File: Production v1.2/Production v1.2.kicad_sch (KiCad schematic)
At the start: 26 parts, among them IC1 MAX3323EEUE+T, J1 530480510, J2 530480410, J3 USB4085-GF-A_REVB, U1 ATSAMD21G18A-AUT, Y1 ECS-.327-12.5-1210-TR

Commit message: 1.2 routed
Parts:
- R4: value 4K7 -> 5K6
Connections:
- net AREFB is gone; now on net AREFA: U1.9 (PA04)
- net +3V3: now also C7.1, U1.17 (VDD/IO), U1.36 (VDD/IO); no longer C7.2
- net GND: now also C7.2; no longer R5.2
- net GNDANA: now also R5.2
- net OLED_CS: now also U1.19 (PB10)
- net OLED_DC: now also U1.15 (PA10); no longer U1.7 (PB08)
- net OLED_RST: now also U1.16 (PA11); no longer U1.8 (PB09)
- net RUN: now also U1.48 (PB03); no longer U1.39 (PA27)
- net SETBTN: now also U1.13 (PA08); no longer U1.3 (PA02)
- net SETLED: now also U1.10 (PA05); no longer U1.48 (PB03)
- net SOFTBTN: now also U1.24 (PA15); no longer U1.14 (PA09)
- net VDDCORE: now reaches C8.1, U1.43 (VDDCORE)

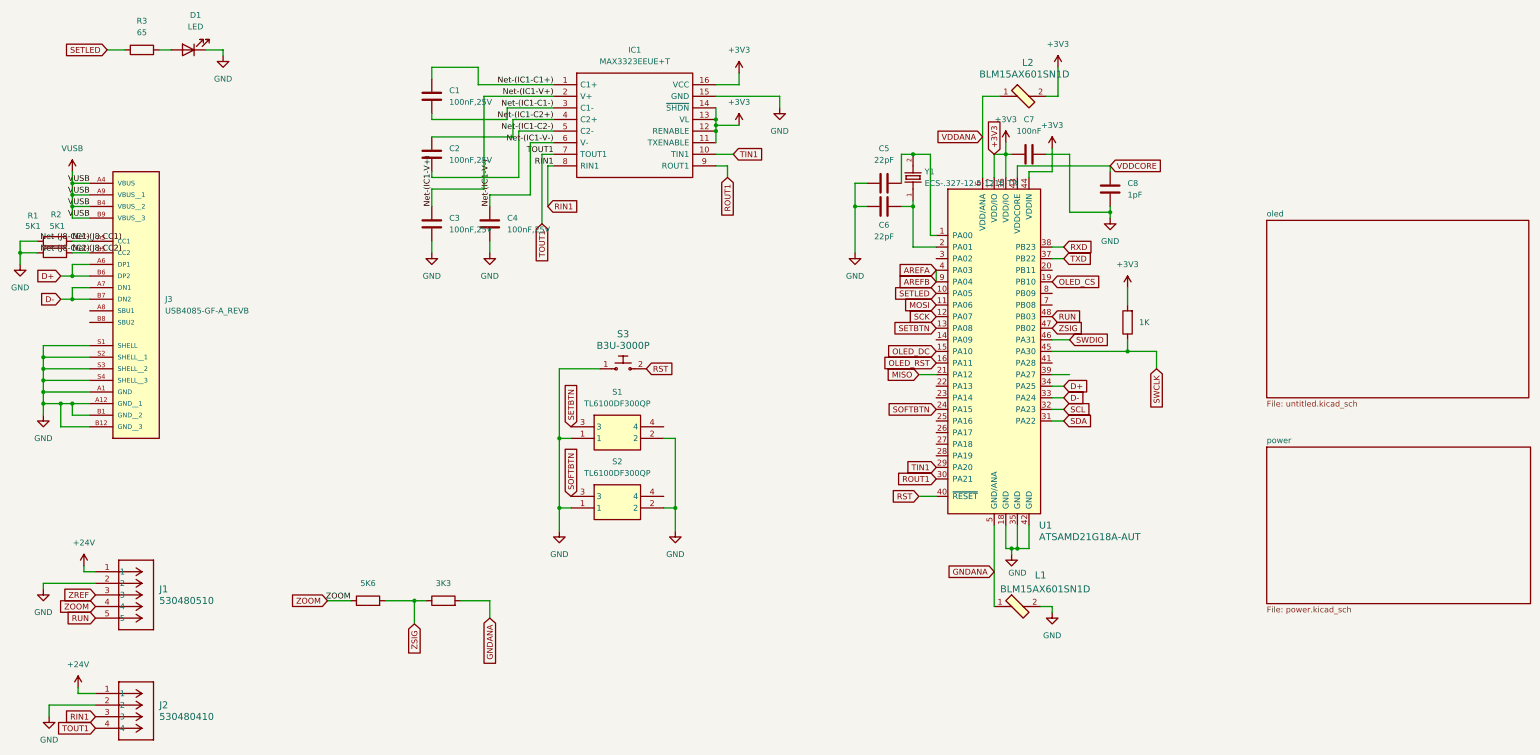
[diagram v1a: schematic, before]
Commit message: v1.2 checked & labeled
flipped fpc connector to underside, for better ribbon routing.
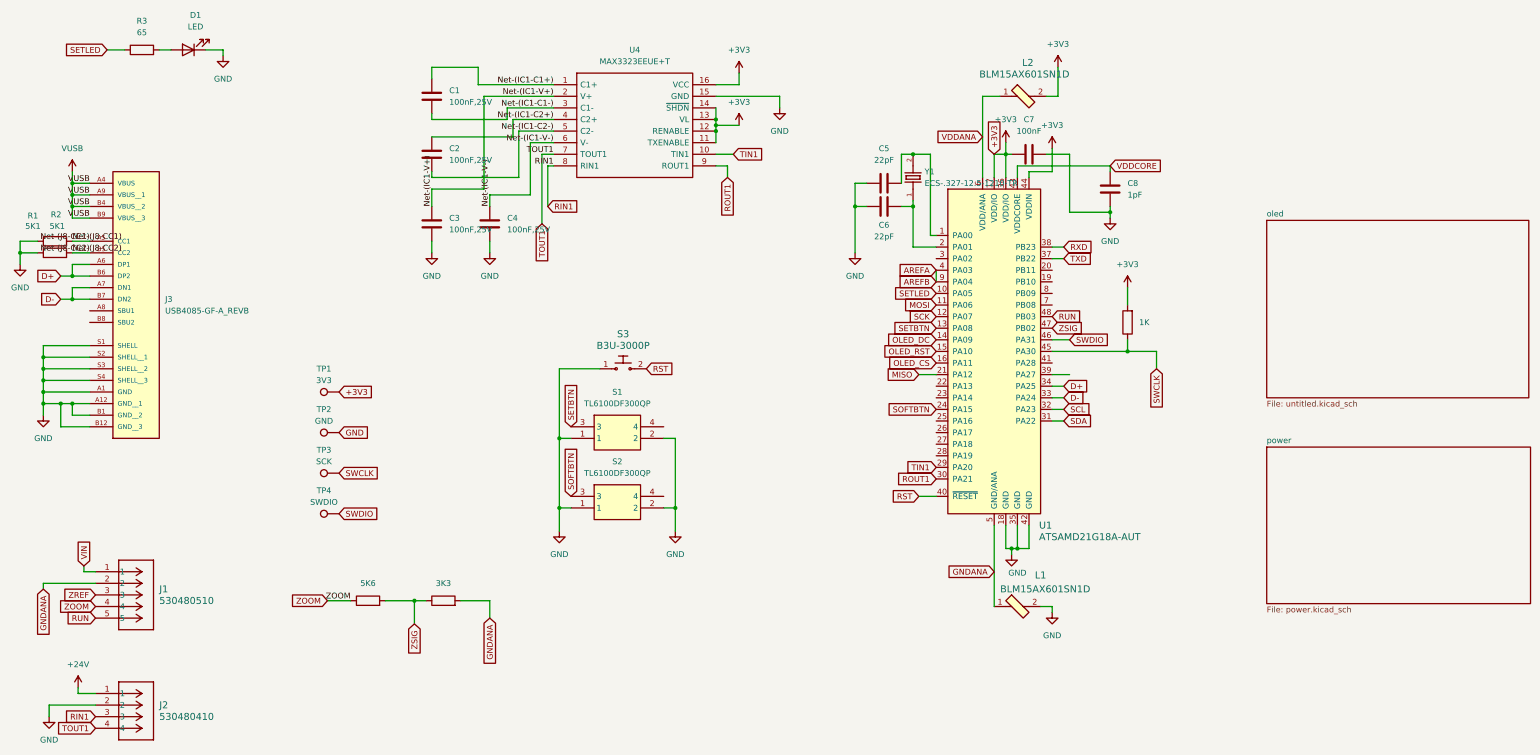
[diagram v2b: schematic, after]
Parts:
- added TP1: 3V3, TestPoint:TestPoint_Pad_1.0x1.0mm, symbol Connector:TestPoint
- added TP2: GND, TestPoint:TestPoint_Pad_1.0x1.0mm, symbol Connector:TestPoint
- added TP3: SCK, TestPoint:TestPoint_Pad_1.0x1.0mm, symbol Connector:TestPoint
- added TP4: SWDIO, TestPoint:TestPoint_Pad_1.0x1.0mm, symbol Connector:TestPoint
- renumbered IC1 to U4
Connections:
- net +24V: no longer J1.1
- net +3V3: now also TP1.1
- net GND: now also TP2.1; no longer J1.2
- net GNDANA: now also J1.2
- net OLED_CS: now also U1.16 (PA11); no longer U1.19 (PB10)
- net OLED_DC: now also U1.14 (PA09); no longer U1.15 (PA10)
- net OLED_RST: now also U1.15 (PA10); no longer U1.16 (PA11)
- net SWCLK: now also TP3.1
- net SWDIO: now also TP4.1
- new net VIN: J1.1

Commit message: Updated some fields
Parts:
- L1, L2: Part Number (none) -> BLM15AX601SN1D; URL (none) -> https://www.digikey.com/en/products/detail/murata-electroni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
- TP1, TP2, TP3, TP4: now not fitted
- Y1: Part Number (none) -> ECS-.327-12.5-1210-TR; URL (none) -> https://www.digikey.com/en/products/detail/ecs-inc/ECS-327-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
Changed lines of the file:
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@@
 			)
 		)
+		(property "Part Number" "BLM15AX601SN1D"
+			(at 248.92 148.59 0)
+			(effects
+				(font
+					(size 1.27 1.27)
+				)
+				(hide yes)
+			)
+		)
+		(property "URL" "https://www.digikey.com/en/products/detail/murata-electronics/BLM15AX601SN1D/2256876?s=N4IgTCBcDaIEIBkCyBGArAQQBoDYAMKAygHIoAiIAugL5A"
+			(at 248.92 148.59 0)
+			(effects
+				(font
+					(size 1.27 1.27)
+				)
+				(hide yes)
+			)
+		)
 		(pin "1"
 		)
@@
 			)
 		)
+		(property "Part Number" "ECS-.327-12.5-1210-TR"
+			(at 226.06 54.61 0)
+			(effects
+				(font
+					(size 1.27 1.27)
+				)
+				(hide yes)
+			)
+		)
+		(property "URL" "https://www.digikey.com/en/products/detail/ecs-inc/ECS-327-12-5-1210-TR/6821602?s=N4IgTCBcDaIKIGEDKBaAdAZjAdhQRjDQFZ8w8AGFAFQCUQBdAXyA"
+			(at 226.06 54.61 0)
+			(effects
+				(font
+					(size 1.27 1.27)
+				)
+				(hide yes)
+			)
+		)
 		(pin "2"
 		)
@@
 		(in_bom yes)
 		(on_board yes)
-		(dnp no)
+		(dnp yes)
 		(fields_autoplaced yes)
 		(property "Reference" "TP2"
@@
 		(in_bom yes)
 		(on_board yes)
-		(dnp no)
+		(dnp yes)
 		(fields_autoplaced yes)
 		(property "Reference" "TP1"
@@
 		(in_bom yes)
 		(on_board yes)
-		(dnp no)
+		(dnp yes)
 		(fields_autoplaced yes)
 		(property "Reference" "TP4"
@@
 		(in_bom yes)
 		(on_board yes)
-		(dnp no)
+		(dnp yes)
 		(fields_autoplaced yes)
 		(property "Reference" "TP3"
@@
 				(hide yes)
 			)
+		)
+		(property "Part Number" "BLM15AX601SN1D"
+			(at 250.19 36.83 0)
+			(effects
+				(font
+					(size 1.27 1.27)
+				)
+				(hide yes)
+			)
+		)
+		(property "URL" "https://www.digikey.com/en/products/detail/murata-electronics/BLM15AX601SN1D/2256876?s=N4IgTCBcDaIEIBkCyBGArAQQBoDYAMKAygHIoAiIAugL5A"
+			(at 250.19 36.83 0)
+			(effects
+				(font
+					(size 1.27 1.27)
+				)
+				(hide yes)
+			)

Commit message: Final tweaks for production v1.2, as manufactured
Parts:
- C7: Part Number CL05C010CB5NNNC -> CL05B104KA5NNNC; URL https://www.digikey.com/en/products/detail/samsung-electro-mechanics/CL05C010CB5NNNC/3887253 -> https://www.digikey.com/en/products/detail/samsung-electro-mechanics/CL05B104KA5NNNC/5961204
- L1: value BLM15AX601SN1D -> 600 MHz @ 100 MHz; Category Filters -> (none); DK_Datasheet_Link https://www.murata.com/en-us/products/productdata/879674159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 -> (none); DK_Detail_Page /product-detail/en/murata-electronics-north-america/BLM18HE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 -> (none); Family Ferrite Beads and Chips -> (none); MPN BLM18HE152SN1D -> (none); Manufacturer Murata Electronics North America -> (none); Part Number BLM15AX601SN1D -> 74269262601; URL https://www.digikey.com/en/products/detail/murata-electroni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 -> https://www.digikey.com/en/products/detail/würth-elektronik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
- L2: value BLM15AX601SN1D -> 600 Ohm @ 100 MHz; Category Filters -> (none); DK_Datasheet_Link https://www.murata.com/en-us/products/productdata/879674159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 -> (none); DK_Detail_Page /product-detail/en/murata-electronics-north-america/BLM18HE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 -> (none); Family Ferrite Beads and Chips -> (none); MPN BLM18HE152SN1D -> (none); Manufacturer Murata Electronics North America -> (none); Part Number BLM15AX601SN1D -> 74269262601; URL https://www.digikey.com/en/products/detail/murata-electroni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 -> https://www.digikey.com/en/products/detail/würth-elektronik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
- R4: footprint Resistor_SMD:R_0201_0603Metric -> Resistor_SMD:R_0402_1005Metric; Part Number ERJ-1GNF4701C -> ERA-2VRW5601X; URL https://www.digikey.com/en/products/detail/panasonic-electronic-components/ERJ-1GNF4701C/2036188 -> https://www.digikey.com/en/products/detail/panasonic-electronic-components/ERA-2VRW5601X/12087670?s=N4IgjCBcoMxaBjKAzAhgGwM4FMA0IB7KAbRADYBOMkAXXwAcAXKEAZUYCcBLAOwHMQAX3xhq0EEkhoseQiRAwKYAKwAOWg2aQ2nXgOHgA7PAkoMOfEUikwAFgAMEOiCYt23fkJEVVFE5OkLOWsQe1oDACZ7VWV-MxlLeWUAOjIAAgBrAHkACwBbTA0XLRAAVR4uRizkAFlsVEwAVw5sLxAAWgi4yE5G2StSWPw-GgN2v3FJXv75J0F5oA
- R5: footprint Resistor_SMD:R_0201_0603Metric -> Resistor_SMD:R_0402_1005Metric; Part Number ERJ-1GNF3301C -> ERA-2VRW3301X; URL https://www.digikey.com/en/products/detail/panasonic-electronic-components/ERJ-1GNF3301C/2036169 -> https://www.digikey.com/en/products/detail/panasonic-electronic-components/ERA-2VRW3301X/12086896?s=N4IgjCBcoMxaBjKAzAhgGwM4FMA0IB7KAbRADYBOMkAXXwAcAXKEAZUYCcBLAOwHMQAX3xhq0EEkhoseQiRAwKYAKwAOWg2aQ2nXgOHgKqivAkoMOfEUikADLQMAmW6uWnJ0y3JsKAdDAACAGsAeQALAFtMDRAmFgBVHi5GEOQAWWxUTABXDmwhfABaR3coTmzZa1I3fBMaA0KTcUlyyvkIesFBIA
- R6: Part Number ERJ-1GNF3301C -> RC0201FR-071KL; URL https://www.digikey.com/en/products/detail/panasonic-electr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 -> https://www.digikey.com/en/products/detail/yageo/RC0201FR-0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
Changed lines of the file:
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@@
 			)
 		)
-		(property "Datasheet" "530480510"
+		(property "Datasheet" ""
 			(at 46.99 140.97 0)
 			(effects
@@
 			)
 		)
-		(property "Value" "BLM15AX601SN1D"
+		(property "Value" "600 MHz @ 100 MHz"
 			(at 255.016 144.78 0)
 			(effects
@@
 			)
 		)
-		(property "Datasheet" "https://www.murata.com/en-us/products/productdata/8796741599262/ENFA0004.pdf"
+		(property "Datasheet" ""
 			(at 254 140.97 0)
 			(effects
@@
 			)
 		)
-		(property "Description" "FERRITE BEAD 1.5 KOHM 0603 1LN"
+		(property "Description" "600 Ohms @ 100 MHz 1 Power Line Ferrite Bead 0603 (1608 Metric) 1.5A 100mOhm"
 			(at 254 123.19 0)
 			(effects
@@
 			)
 		)
-		(property "MPN" "BLM18HE152SN1D"
-			(at 254 135.89 0)
-			(effects
-				(font
-					(size 1.524 1.524)
-				)
-				(justify left)
-				(hide yes)
-			)
-		)
-		(property "Category" "Filters"
-			(at 254 133.35 0)
-			(effects
-				(font
-					(size 1.524 1.524)
-				)
-				(justify left)
-				(hide yes)
-			)
-		)
-		(property "Family" "Ferrite Beads and Chips"
-			(at 254 130.81 0)
-			(effects
-				(font
-					(size 1.524 1.524)
-				)
-				(justify left)
-				(hide yes)
-			)
-		)
-		(property "DK_Datasheet_Link" "https://www.murata.com/en-us/products/productdata/8796741599262/ENFA0004.pdf"
-			(at 254 128.27 0)
-			(effects
-				(font
-					(size 1.524 1.524)
-				)
-				(justify left)
-				(hide yes)
-			)
-		)
-		(property "DK_Detail_Page" "/product-detail/en/murata-electronics-north-america/BLM18HE152SN1D/490-5216-1-ND/1948392"
-			(at 254 125.73 0)
-			(effects
-				(font
-					(size 1.524 1.524)
-				)
-				(justify left)
-				(hide yes)
-			)
-		)
-		(property "Manufacturer" "Murata Electronics North America"
-			(at 254 120.65 0)
-			(effects
-				(font
-					(size 1.524 1.524)
-				)
-				(justify left)
-				(hide yes)
-			)
-		)
 		(property "Status" "Active"
 			(at 254 118.11 0)
@@
 			)
 		)
-		(property "Part Number" "BLM15AX601SN1D"
+		(property "Part Number" "74269262601"
 			(at 248.92 148.59 0)
 			(effects
@@
 			)
 		)
-		(property "URL" "https://www.digikey.com/en/products/detail/murata-electronics/BLM15AX601SN1D/2256876?s=N4IgTCBcDaIEIBkCyBGArAQQBoDYAMKAygHIoAiIAugL5A"
+		(property "URL" "https://www.digikey.com/en/products/detail/würth-elektronik/74269262601/17829853"
 			(at 248.92 148.59 0)
 			(effects
@@
 			)
 		)
-		(property "Datasheet" "https://componentsearchengine.com/Datasheets/2/MAX3323EEPE+.pdf"
+		(property "Datasheet" ""
 			(at 179.07 34.29 0)
 			(effects
@@
 			)
 		)
-		(property "Part Number" "ERJ-1GNF3301C"
+		(property "Part Number" "RC0201FR-071KL"
 			(at 273.05 86.36 0)
 			(effects
@@
 			)
 		)
-		(property "URL" "https://www.digikey.com/en/products/detail/panasonic-electronic-components/ERJ-1GNF3301C/2036169"
+		(property "URL" "https://www.digikey.com/en/products/detail/yageo/RC0201FR-071KL/3202389"
 			(at 273.05 86.36 0)
 			(effects
@@
 			)
 		)
-		(property "Part Number" "CL05C010CB5NNNC"
+		(property "Part Number" "CL05B104KA5NNNC"
 			(at 251.46 49.53 0)
 			(effects
@@
 			)
 		)
-		(property "URL" "https://www.digikey.com/en/products/detail/samsung-electro-mechanics/CL05C010CB5NNNC/3887253"
+		(property "URL" "https://www.digikey.com/en/products/detail/samsung-electro-mechanics/CL05B104KA5NNNC/5961204"
 			(at 251.46 49.53 0)
 			(effects
@@
 			)
 		)
-		(property "Datasheet" "https://configured-product-images.s3.amazonaws.com/2D/specs/TL6100AF300QP.pdf"
+		(property "Datasheet" ""
 			(at 167.64 304.14 0)
 			(effects
@@
 			)
 		)
-		(property "Datasheet" "https://omronfs.omron.com/en_US/ecb/products/pdf/en-b3u.pdf"
+		(property "Datasheet" ""
 			(at 167.64 88.9 0)
 			(effects
@@
 			)
 		)
-		(property "Footprint" "Resistor_SMD:R_0201_0603Metric"
+		(property "Footprint" "Resistor_SMD:R_0402_1005Metric"
 			(at 106.68 149.098 90)
 			(effects
@@
 			)
 		)
-		(property "Part Number" "ERJ-1GNF4701C"
+		(property "Part Number" "ERA-2VRW5601X"
 			(at 106.68 147.32 0)
 			(effects
@@
 			)
 		)
-		(property "URL" "https://www.digikey.com/en/products/detail/panasonic-electronic-components/ERJ-1GNF4701C/2036188"
+		(property "URL" "https://www.digikey.com/en/products/detail/panasonic-electronic-components/ERA-2VRW5601X/12087670?s=N4IgjCBcoMxaBjKAzAhgGwM4FMA0IB7KAbRADYBOMkAXXwAcAXKEAZUYCcBLAOwHMQAX3xhq0EEkhoseQiRAwKYAKwAOWg2aQ2nXgOHgA7PAkoMOfEUikwAFgAMEOiCYt23fkJEVVFE5OkLOWsQe1oDACZ7VWV-MxlLeWUAOjIAAgBrAHkACwBbTA0XLRAAVR4uRizkAFlsVEwAVw5sLxAAWgi4yE5G2StSWPw-GgN2v3FJXv75J0F5oA"
 			(at 106.68 147.32 0)
 			(effects
@@
 			)
 		)
-		(property "Footprint" "Resistor_SMD:R_0201_0603Metric"
+		(property "Footprint" "Resistor_SMD:R_0402_1005Metric"
 			(at 123.19 149.098 90)
 			(effects
@@
 			)
 		)
-		(property "Part Number" "ERJ-1GNF3301C"
+		(property "Part Number" "ERA-2VRW3301X"
 			(at 123.19 147.32 0)
 			(effects
@@
 			)
 		)
-		(property "URL" "https://www.digikey.com/en/products/detail/panasonic-electronic-components/ERJ-1GNF3301C/2036169"
+		(property "URL" "https://www.digikey.com/en/products/detail/panasonic-electronic-components/ERA-2VRW3301X/12086896?s=N4IgjCBcoMxaBjKAzAhgGwM4FMA0IB7KAbRADYBOMkAXXwAcAXKEAZUYCcBLAOwHMQAX3xhq0EEkhoseQiRAwKYAKwAOWg2aQ2nXgOHgKqivAkoMOfEUikADLQMAmW6uWnJ0y3JsKAdDAACAGsAeQALAFtMDRAmFgBVHi5GEOQAWWxUTABXDmwhfABaR3coTmzZa1I3fBMaA0KTcUlyyvkIesFBIA"
 			(at 123.19 147.32 0)
 			(effects
@@
 			)
 		)
-		(property "Datasheet" "http://www.microchip.com/mymicrochip/filehandler.aspx?ddocname=en605782"
+		(property "Datasheet" ""
 			(at 248.92 87.63 0)
 			(effects
@@
 			)
 		)
-		(property "Value" "BLM15AX601SN1D"
+		(property "Value" "600 Ohm @ 100 MHz"
 			(at 250.444 32.004 0)
 			(effects
@@
 			)
 		)
-		(property "Datasheet" "https://www.murata.com/en-us/products/productdata/8796741599262/ENFA0004.pdf"
+		(property "Datasheet" ""
 			(at 255.27 29.21 0)
 			(effects
@@
 			)
 		)
-		(property "Description" "FERRITE BEAD 1.5 KOHM 0603 1LN"
+		(property "Description" "600 Ohms @ 100 MHz 1 Power Line Ferrite Bead 0603 (1608 Metric) 1.5A 100mOhm"
 			(at 255.27 11.43 0)
 			(effects
@@
 			)
 		)
-		(property "MPN" "BLM18HE152SN1D"
-			(at 255.27 24.13 0)
-			(effects
-				(font
-					(size 1.524 1.524)
-				)
-				(justify left)
-				(hide yes)
-			)
-		)
-		(property "Category" "Filters"
-			(at 255.27 21.59 0)
-			(effects
-				(font
-					(size 1.524 1.524)
-				)
-				(justify left)
-				(hide yes)
-			)
-		)
-		(property "Family" "Ferrite Beads and Chips"
-			(at 255.27 19.05 0)
-			(effects
-				(font
-					(size 1.524 1.524)
-				)
-				(justify left)
-				(hide yes)
-			)
-		)
-		(property "DK_Datasheet_Link" "https://www.murata.com/en-us/products/productdata/8796741599262/ENFA0004.pdf"
-			(at 255.27 16.51 0)
-			(effects
-				(font
-					(size 1.524 1.524)
-				)
-				(justify left)
-				(hide yes)
-			)
-		)
-		(property "DK_Detail_Page" "/product-detail/en/murata-electronics-north-america/BLM18HE152SN1D/490-5216-1-ND/1948392"
-			(at 255.27 13.97 0)
-			(effects
-				(font
-					(size 1.524 1.524)
-				)
-				(justify left)
-				(hide yes)
-			)
-		)
-		(property "Manufacturer" "Murata Electronics North America"
-			(at 255.27 8.89 0)
-			(effects
-				(font
-					(size 1.524 1.524)
-				)
-				(justify left)
-				(hide yes)
-			)
-		)
 		(property "Status" "Active"
 			(at 255.27 6.35 0)
@@
 			)
 		)
-		(property "Part Number" "BLM15AX601SN1D"
+		(property "Part Number" "74269262601"
 			(at 250.19 36.83 0)
 			(effects
@@
 			)
 		)
-		(property "URL" "https://www.digikey.com/en/products/detail/murata-electronics/BLM15AX601SN1D/2256876?s=N4IgTCBcDaIEIBkCyBGArAQQBoDYAMKAygHIoAiIAugL5A"
+		(property "URL" "https://www.digikey.com/en/products/detail/würth-elektronik/74269262601/17829853"
 			(at 250.19 36.83 0)
 			(effects
@@
 			)
 		)
-		(property "Datasheet" "530480410"
+		(property "Datasheet" ""
 			(at 46.99 167.64 0)
 			(effects
@@
 			)
 		)
-		(property "Datasheet" "https://configured-product-images.s3.amazonaws.com/2D/specs/TL6100AF300QP.pdf"
+		(property "Datasheet" ""
 			(at 167.64 319.38 0)
 			(effects
